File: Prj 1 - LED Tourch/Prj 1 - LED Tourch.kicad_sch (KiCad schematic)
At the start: 4 parts, among them SW1 SW_DIP_x01

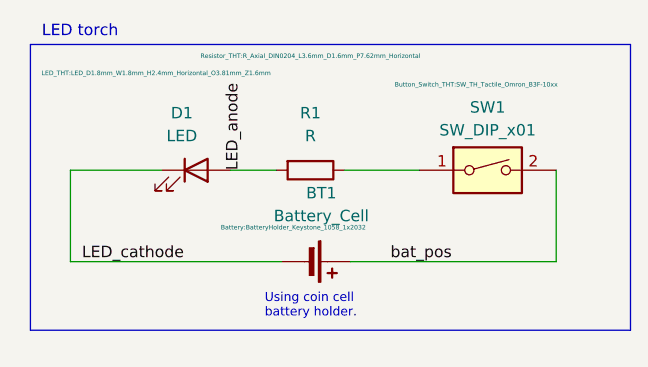
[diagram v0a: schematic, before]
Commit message: update to include routing
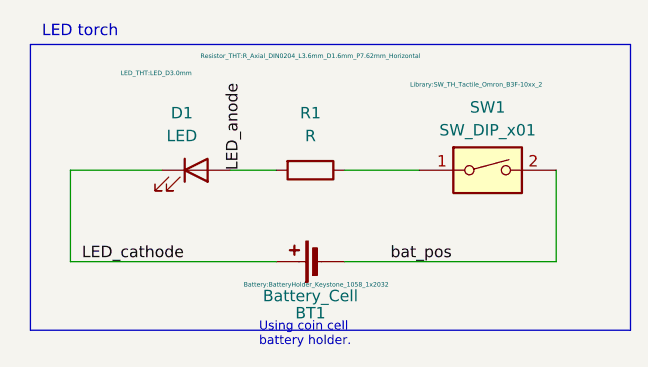
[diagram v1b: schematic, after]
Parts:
- D1: footprint LED_THT:LED_D1.8mm_W1.8mm_H2.4mm_Horizontal_O3.81mm_Z1.6mm -> LED_THT:LED_D3.0mm
- SW1: footprint Button_Switch_THT:SW_TH_Tactile_Omron_B3F-10xx -> Library:SW_TH_Tactile_Omron_B3F-10xx_2
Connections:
- net LED_cathode: now also BT1.1 (+); no longer BT1.2 (-)
- net bat_pos: now also BT1.2 (-); no longer BT1.1 (+)
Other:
- moved on the sheet: BT1
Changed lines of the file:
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@@
     (stroke (width 0) (type default))
   )
-  (wire (pts (xy 125.73 91.44) (xy 148.59 91.44))
+  (wire (pts (xy 125.095 91.44) (xy 148.59 91.44))
     (stroke (width 0) (type default))
   )
@@
     (stroke (width 0) (type default))
   )
-  (wire (pts (xy 118.11 91.44) (xy 94.615 91.44))
+  (wire (pts (xy 94.615 91.44) (xy 117.475 91.44))
     (stroke (width 0) (type default))
   )
@@
     (effects (font (size 1.27 1.27)) (justify left bottom))
   )
-  (text "Using coin cell\nbattery holder." (at 116.205 97.79 0)
+  (text "Using coin cell\nbattery holder." (at 115.57 100.965 0)
     (effects (font (size 1 1)) (justify left bottom))
   )
@@
       (effects (font (size 1.27 1.27)))
     )
-    (property "Footprint" "Button_Switch_THT:SW_TH_Tactile_Omron_B3F-10xx" (at 139.7 71.755 0)
+    (property "Footprint" "Library:SW_TH_Tactile_Omron_B3F-10xx_2" (at 139.7 71.755 0)
       (effects (font (size 0.5 0.5)))
     )
@@
       (effects (font (size 1.27 1.27)))
     )
-    (property "Footprint" "LED_THT:LED_D1.8mm_W1.8mm_H2.4mm_Horizontal_O3.81mm_Z1.6mm" (at 104.14 70.485 0)
+    (property "Footprint" "LED_THT:LED_D3.0mm" (at 104.14 70.485 0)
       (effects (font (size 0.5 0.5)))
     )
@@
     )
   )
-  (symbol (lib_id "Device:Battery_Cell") (at 120.65 91.44 270) (unit 1)
+  (symbol (lib_id "Device:Battery_Cell") (at 122.555 91.44 90) (unit 1)
     (in_bom yes) (on_board yes) (dnp no)
-    (property "Reference" "BT1" (at 122.4915 83.82 90)
+    (property "Reference" "BT1" (at 121.285 97.155 90)
       (effects (font (size 1.27 1.27)))
     )
-    (property "Value" "Battery_Cell" (at 122.4915 86.36 90)
+    (property "Value" "Battery_Cell" (at 121.285 95.25 90)
       (effects (font (size 1.27 1.27)))
     )
-    (property "Footprint" "Battery:BatteryHolder_Keystone_1058_1x2032" (at 119.38 87.63 90)
+    (property "Footprint" "Battery:BatteryHolder_Keystone_1058_1x2032" (at 121.92 93.98 90)
       (effects (font (size 0.5 0.5)))
     )
-    (property "Datasheet" "~" (at 122.174 91.44 90)
+    (property "Datasheet" "~" (at 121.031 91.44 90)
       (effects (font (size 0.5 0.5)) hide)
     )

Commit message: cut the edge for the battery
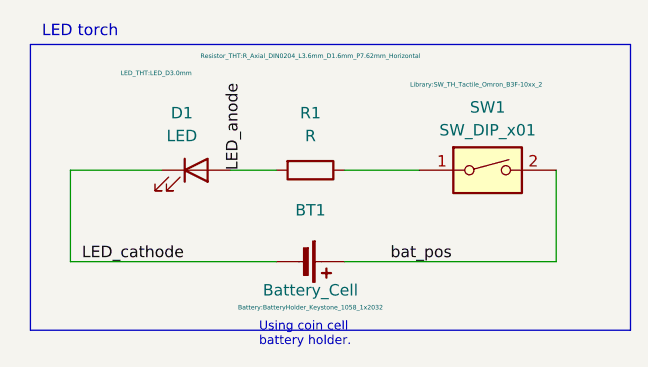
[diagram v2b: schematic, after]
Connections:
- net LED_cathode: now also BT1.2 (-); no longer BT1.1 (+)
- net bat_pos: now also BT1.1 (+); no longer BT1.2 (-)
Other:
- moved on the sheet: BT1
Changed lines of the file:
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@@
     )
   )
-  (symbol (lib_id "Device:Battery_Cell") (at 122.555 91.44 90) (unit 1)
+  (symbol (lib_id "Device:Battery_Cell") (at 120.015 91.44 270) (unit 1)
     (in_bom yes) (on_board yes) (dnp no)
-    (property "Reference" "BT1" (at 121.285 97.155 90)
+    (property "Reference" "BT1" (at 121.285 85.725 90)
       (effects (font (size 1.27 1.27)))
     )
-    (property "Value" "Battery_Cell" (at 121.285 95.25 90)
+    (property "Value" "Battery_Cell" (at 121.285 94.615 90)
       (effects (font (size 1.27 1.27)))
     )
-    (property "Footprint" "Battery:BatteryHolder_Keystone_1058_1x2032" (at 121.92 93.98 90)
+    (property "Footprint" "Battery:BatteryHolder_Keystone_1058_1x2032" (at 121.285 96.52 90)
       (effects (font (size 0.5 0.5)))
     )
-    (property "Datasheet" "~" (at 121.031 91.44 90)
+    (property "Datasheet" "~" (at 121.539 91.44 90)
       (effects (font (size 0.5 0.5)) hide)
     )
